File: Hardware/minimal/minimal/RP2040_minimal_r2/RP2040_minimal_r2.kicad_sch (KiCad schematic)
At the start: 27 parts, among them J3 Conn_02x18_Odd_Even, J4 Conn_02x18_Odd_Even, SW1 TL3342F160QG_TR, U3 RP2040, U3 W25Q128JVS, Y1 12Mhz

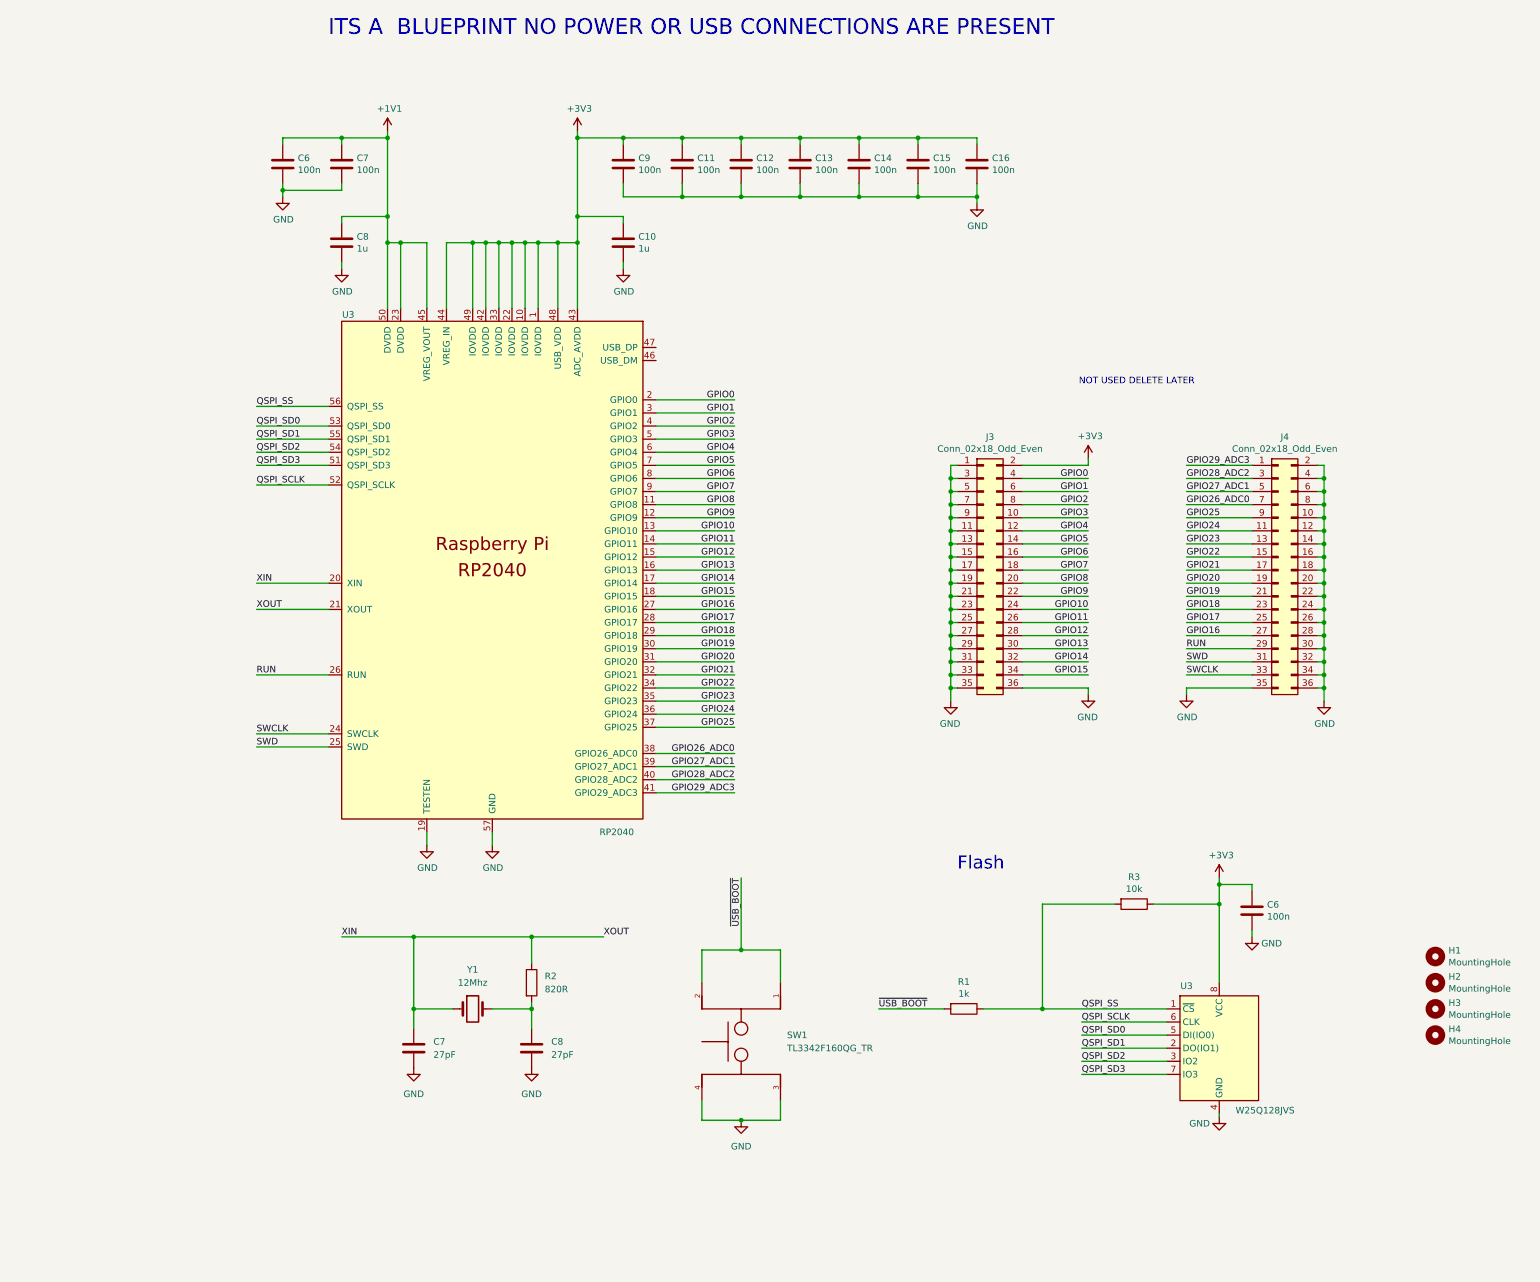
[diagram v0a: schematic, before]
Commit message: Added Buck and Boost converter as well as a basic RP2040 circuit
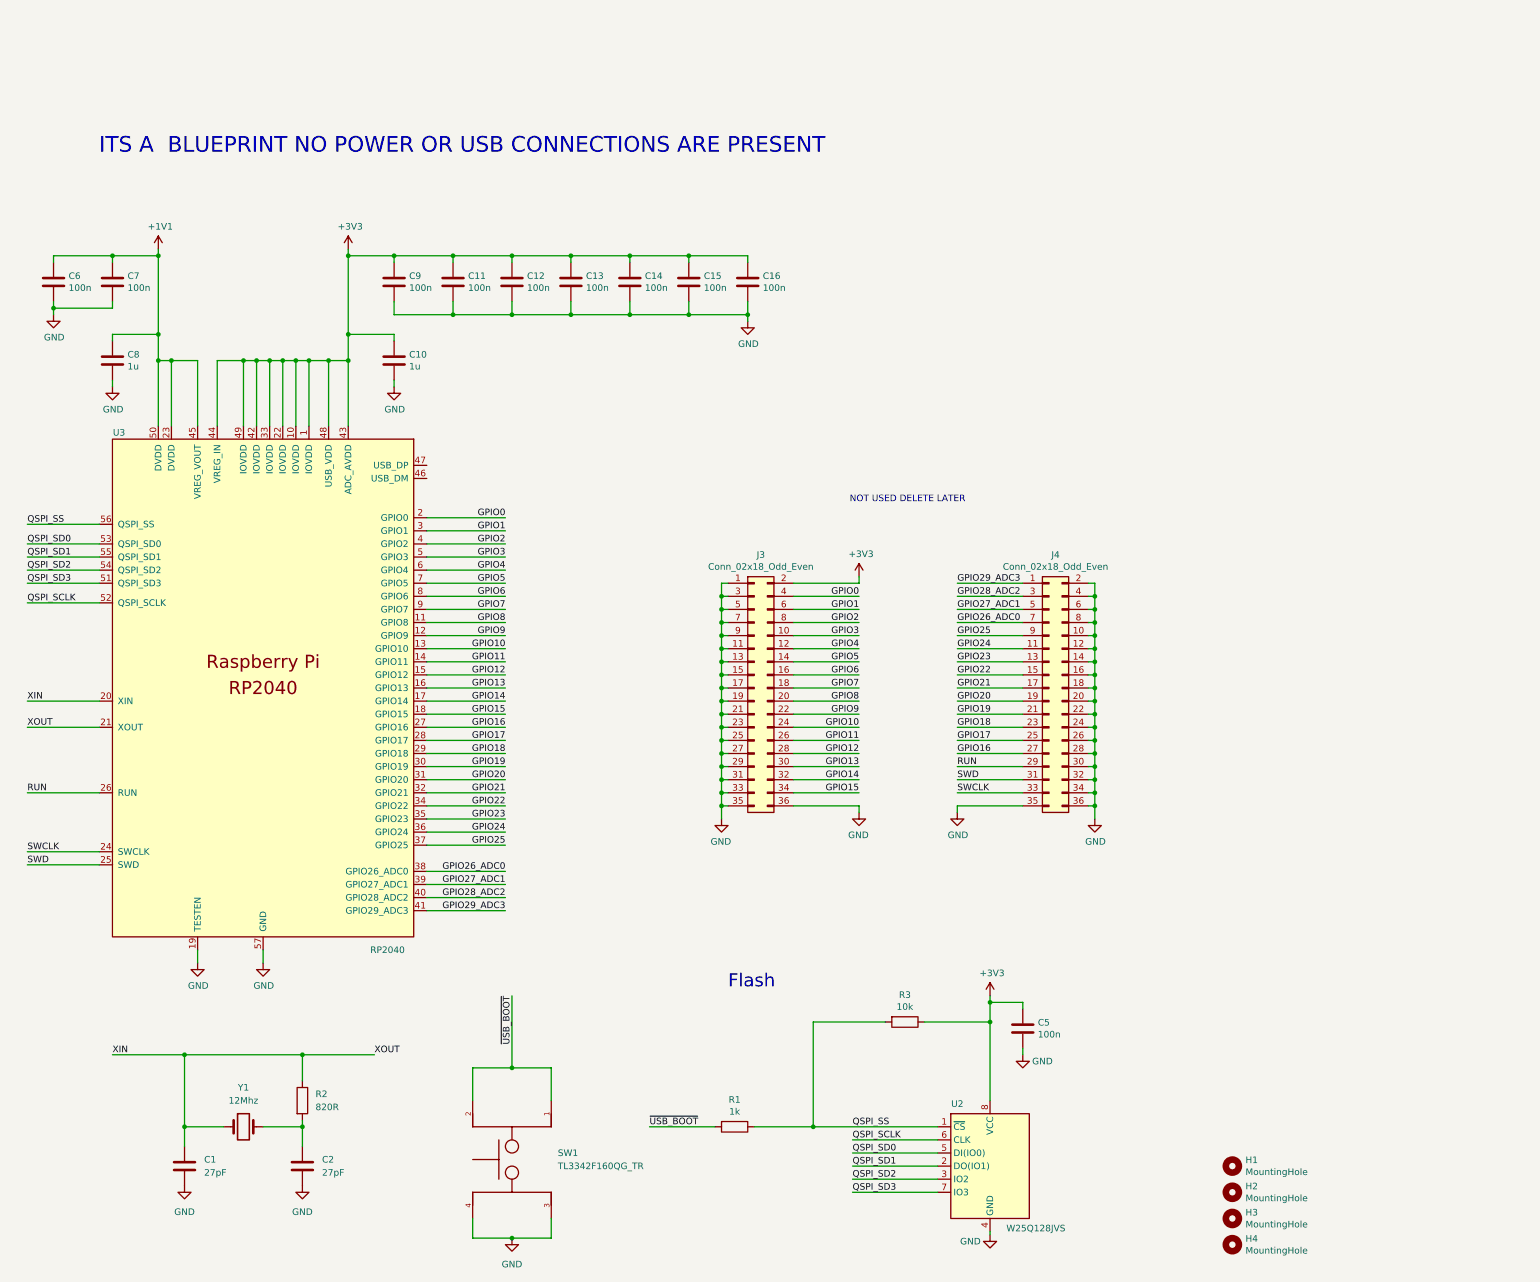
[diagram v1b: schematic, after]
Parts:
- removed C6: 100n, Capacitor_SMD:C_0603_1608Metric_Pad1.08x0.95mm_HandSolder, symbol Device:C
- removed C7, C8: 27pF, Capacitor_SMD:C_0603_1608Metric_Pad1.08x0.95mm_HandSolder, symbol Device:C
- removed U3: W25Q128JVS, Package_SO:SOIC-8_5.23x5.23mm_P1.27mm, symbol Memory_Flash:W25Q128JVS
- added C1, C2: 27pF, Capacitor_SMD:C_0603_1608Metric_Pad1.08x0.95mm_HandSolder, symbol Device:C
- added C5: 100n, Capacitor_SMD:C_0603_1608Metric_Pad1.08x0.95mm_HandSolder, symbol Device:C
- added U2: W25Q128JVS, Package_SO:SOIC-8_5.23x5.23mm_P1.27mm, symbol Memory_Flash:W25Q128JVS
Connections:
- net +3V3: now also C5.1, U2.8 (VCC)
- net GND: now also C1.2, C2.2, C5.2, U2.4 (GND)
- net QSPI_SCLK: now also U2.6 (CLK)
- net QSPI_SD0: now also U2.5 (DI(IO0))
- net QSPI_SD1: now also U2.2 (DO(IO1))
- net QSPI_SD2: now also U2.3 (IO2)
- net QSPI_SD3: now also U2.7 (IO3)
- net QSPI_SS: now also U2.1 (~{CS})
- net XIN: now also C1.1
- net at R2.2, Y1.2: now also C2.1
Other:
- company: (none) -> Raspberry Pi Ltd
- title: (none) -> RP2040 Minimal Design Example
- moved on the sheet: C10, C11, C12, C13, C14, C15, C16, C6, C7, C8, C9, H1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
